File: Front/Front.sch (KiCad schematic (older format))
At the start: 41 parts, among them J1 USB_B_Micro, Q1 BC849, Q2 BC849, SW2 SW_Push, U1 CH340C, U10 ESP32-WROOM-32, U2 CJVL53L0XV2, U3 SPX3819M5-L-3-3

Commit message: V0.2: Redo front schematic and PCB
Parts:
- removed D1: BLUE, LED_SMD:LED_0805_2012Metric_Pad1.15x1.40mm_HandSolder, symbol Device:LED
- removed D2: GREEN, LED_SMD:LED_0805_2012Metric_Pad1.15x1.40mm_HandSolder, symbol Device:LED
- removed H17: VBS, Custom:Mounting_Pad_Power, symbol Front-rescue:MountingPad-Custom
- removed SW2: SW_Push, Button_Switch_SMD:Panasonic_EVQPUJ_EVQPUA, symbol Switch:SW_Push
- added H25: LED1, Custom:Mounting_Pad_Signal, symbol Front-rescue:MountingPad-Custom
- added H26: LED2, Custom:Mounting_Pad_Signal, symbol Front-rescue:MountingPad-Custom
- added H27: TCH2, Custom:Mounting_Pad_Touch, symbol Front-rescue:MountingPad-Custom
- added H28: TCH1, Custom:Mounting_Pad_Touch, symbol Front-rescue:MountingPad-Custom
- added SW1: SW_DPDT_x2, Custom:JS102011SAQN, symbol Switch:SW_DPDT_x2
- H1: value VBUS -> PWR
- H16: value ORST -> O~RST
- R3, R4: value 150 -> 510
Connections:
- net ED_IN1: now also U10.4 (SENSOR_VP); no longer U10.12 (IO27)
- net ED_IN2: now also U10.5 (SENSOR_VN); no longer U10.27 (IO16)
- net M1_AOUT1: now also U10.16 (IO13); no longer U10.19 (SCS/CMD)
- net M1_AOUT2: now also U10.12 (IO27); no longer U10.18 (SWP/SD3)
- net M1_BOUT1: now also U10.13 (IO14); no longer U10.17 (SHD/SD2)
- net M1_BOUT2: now also U10.14 (IO12); no longer U10.16 (IO13)
- net M1_M2_~SLEEP: now also U10.28 (IO17); no longer U10.24 (IO2)
- net M2_AOUT1: now also U10.23 (IO15); no longer U10.20 (SCK/CLK)
- net M2_AOUT2: now also U10.24 (IO2); no longer U10.21 (SDO/SD0)
- net M2_BOUT1: now also U10.26 (IO4); no longer U10.22 (SDI/SD1)
- net M2_BOUT2: now also U10.27 (IO16); no longer U10.23 (IO15)
- net OD_INTERRUPT: now also U10.7 (IO35); no longer U10.31 (IO19)
- net OD_SCL: now also U10.29 (IO5); no longer U10.28 (IO17)
- net OD_SDA: now also U10.30 (IO18); no longer U10.29 (IO5)
- net OD_SHUT: now also U10.31 (IO19); no longer U10.30 (IO18)
- net VBUS: now also SW1.1 (A); no longer U3.1 (IN), U3.3 (EN)
- net LED1: now reaches U10.10 (IO25)
- net LED1: now also H25.1 (Pin)
- net LED2: now reaches U10.11 (IO26)
- net LED2: now also H26.1 (Pin)
- net TOUCH2: now reaches U10.9 (IO33)
- net TOUCH2: now also R4.2
- net TOUCH1: now reaches R3.1
- net TOUCH1: now also U10.8 (IO32)
- net at R4.1: now also H27.1 (Pin)
- net STATUS_LED_BLUE: no longer names the net of R3.2
- net STATUS_LED_BLUE: now also H28.1 (Pin); no longer U10.8 (IO32)
- removed net STATUS_LED_GRN: R4.2, U10.7 (IO35)
- new net: SW1.2 (B), U3.1 (IN), U3.3 (EN)
- no-connect marks 17 -> 16
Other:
- note removed: "Status LEDS"
- moved on the sheet: C2, H1, H10, H11, H12, H13, H14, H15, H16, H18, H19, H2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

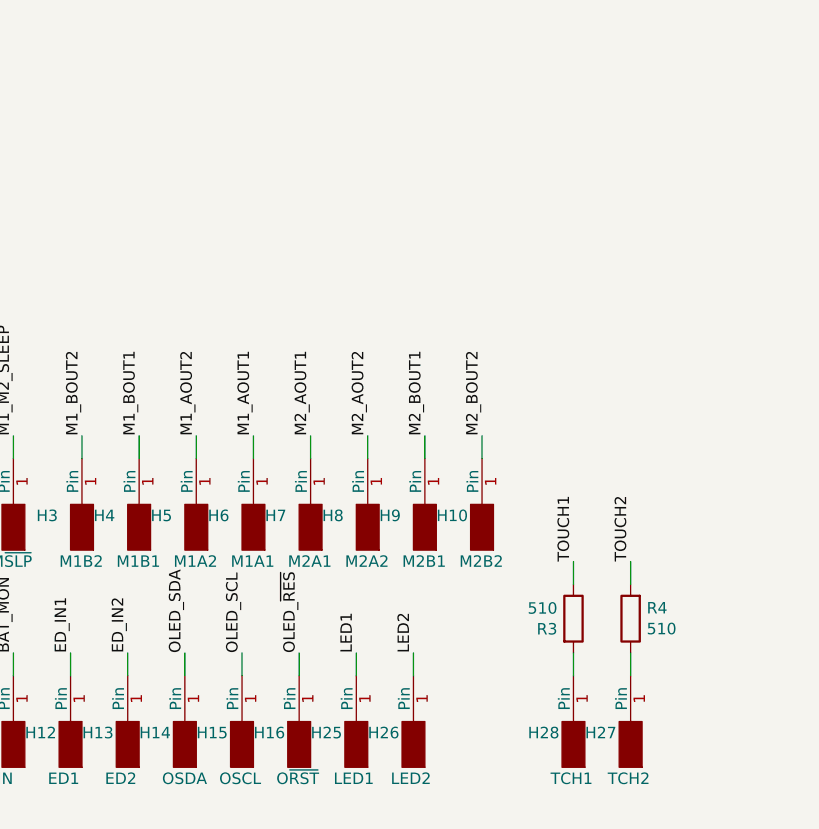
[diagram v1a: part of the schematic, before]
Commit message: finish top, changes to front, added graphic
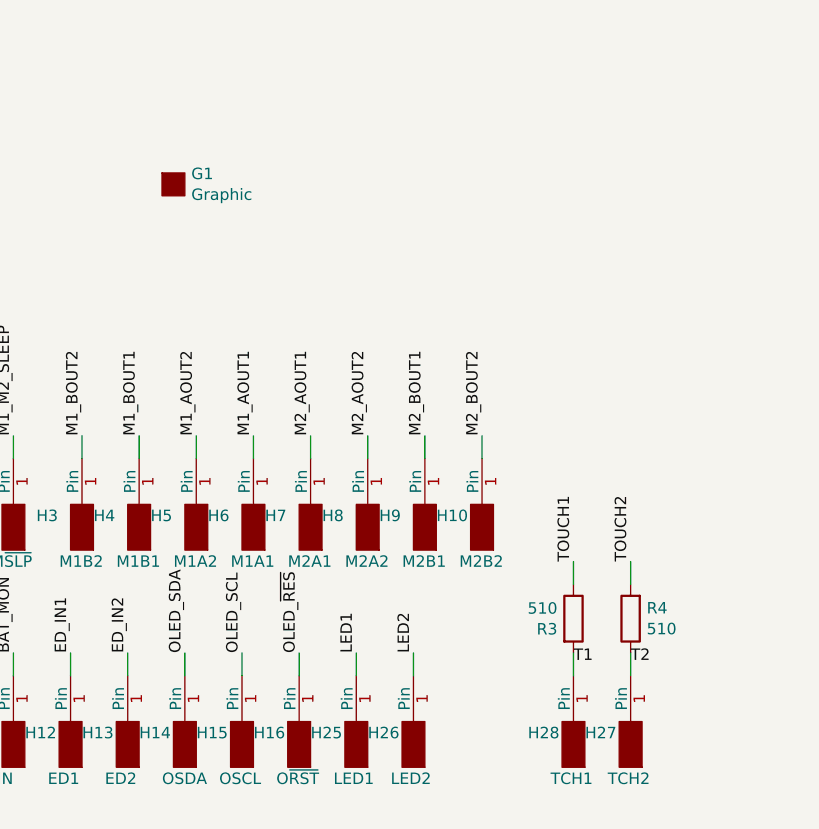
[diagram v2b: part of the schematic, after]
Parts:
- added G1: Graphic, Print:d1, symbol Custom:Graphic
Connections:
- net T2: now reaches H27.1 (Pin), R4.1
- net T1: now reaches H28.1 (Pin), R3.2
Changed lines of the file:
@@
 Text Label 3700 6250 1    50   ~ 0
 TOUCH2
+Text Label 3450 6700 0    50   ~ 0
+T1
+Text Label 3700 6700 0    50   ~ 0
+T2
+$Comp
+L Custom:Graphic G1
+U 1 1 5DEC1C54
+P 1700 4600
+F 0 "G1" H 1778 4646 50  0000 L CNN
+F 1 "Graphic" H 1778 4555 50  0000 L CNN
+F 2 "Print:d1" H 1550 4750 50  0001 C CNN
+F 3 "" H 1550 4750 50  0001 C CNN
+	1    1700 4600
+	1    0    0    -1
+$EndComp
 $EndSCHEMATC

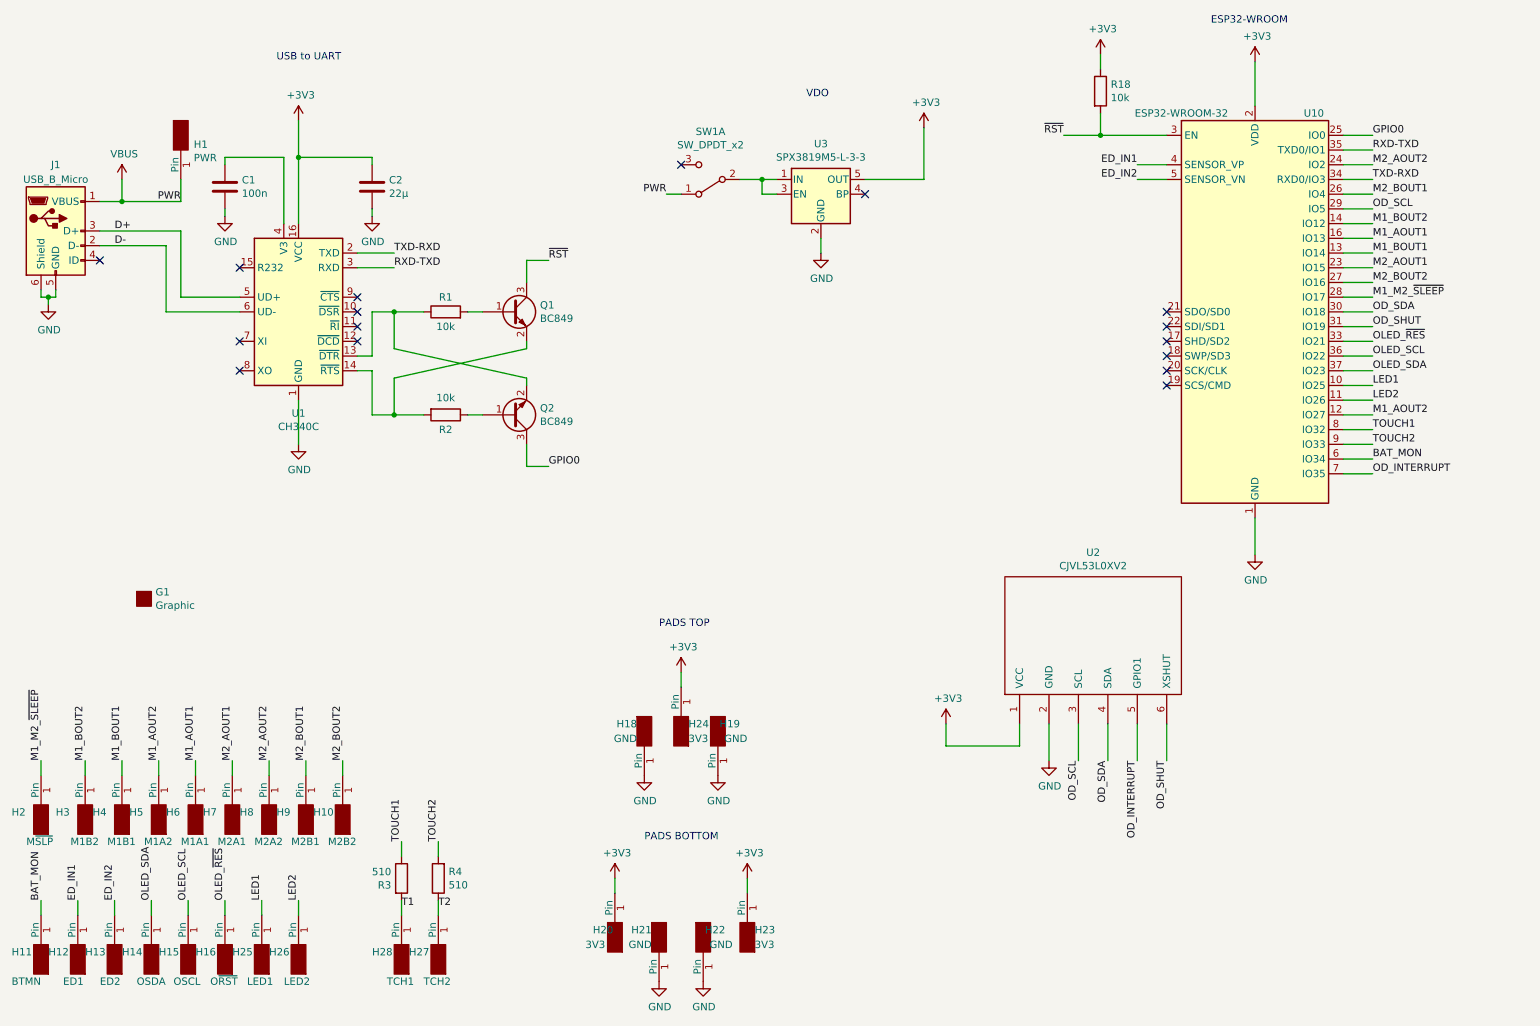
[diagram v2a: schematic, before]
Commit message: removed extra pins in front, respaced pins in bottom and front
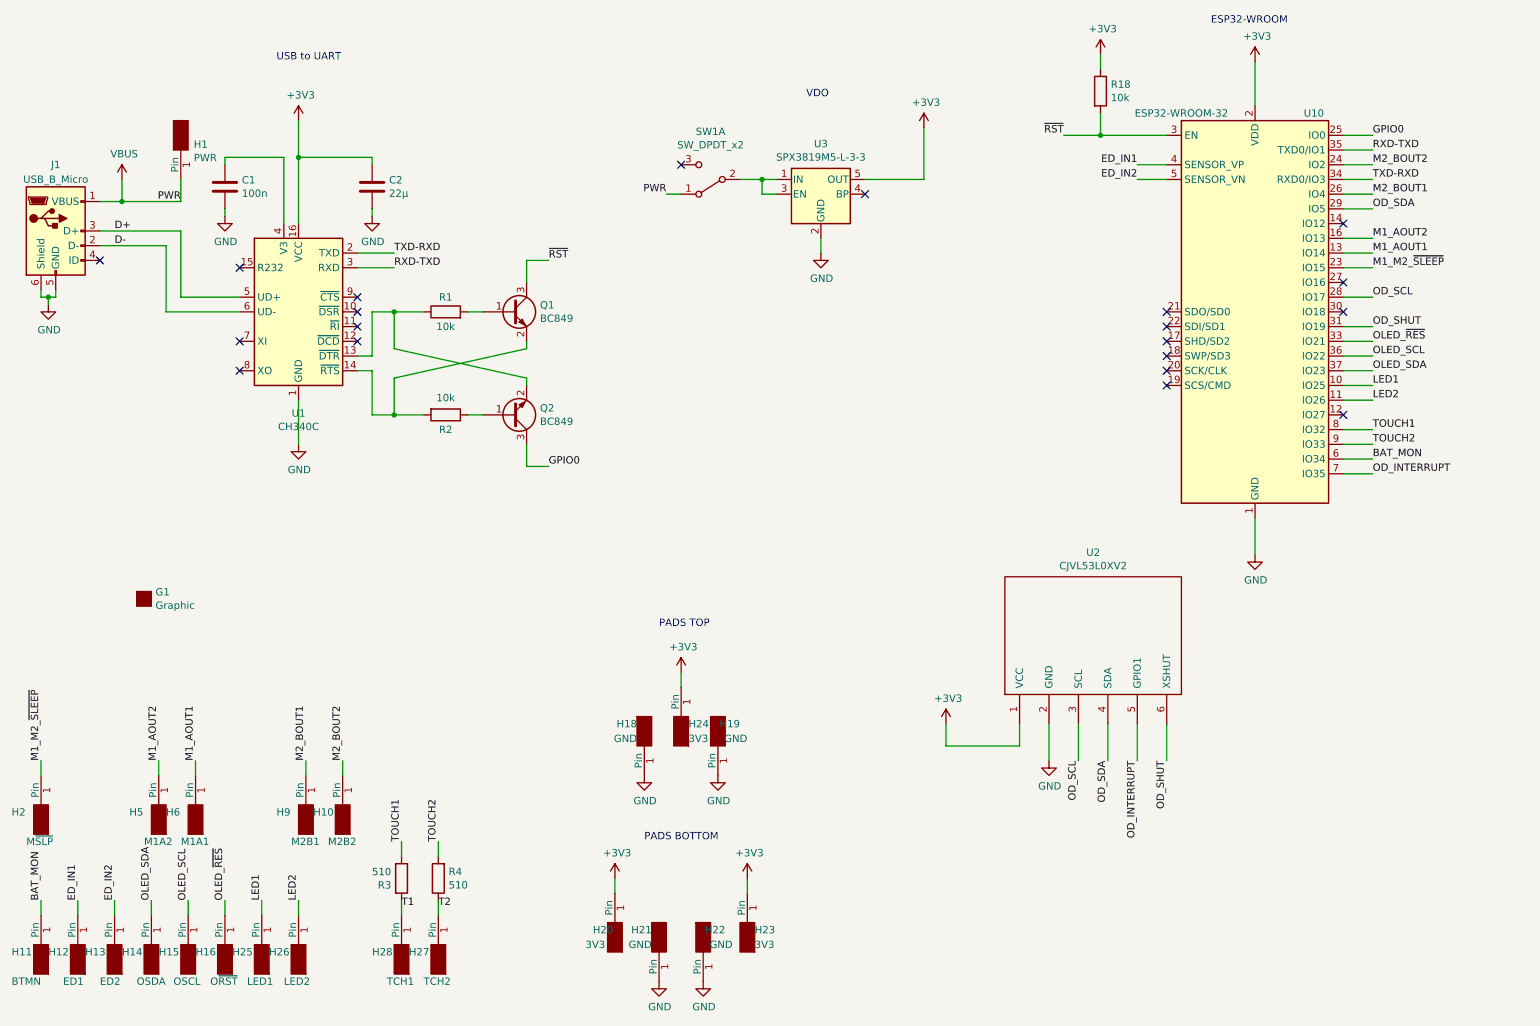
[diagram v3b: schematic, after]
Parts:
- removed H3: M1B2, Custom:Mounting_Pad_Signal, symbol Front-rescue:MountingPad-Custom
- removed H4: M1B1, Custom:Mounting_Pad_Signal, symbol Front-rescue:MountingPad-Custom
- removed H7: M2A1, Custom:Mounting_Pad_Signal, symbol Front-rescue:MountingPad-Custom
- removed H8: M2A2, Custom:Mounting_Pad_Signal, symbol Front-rescue:MountingPad-Custom
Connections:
- net M1_BOUT1 is gone; now on net M1_AOUT1: U10.13 (IO14)
- net M2_AOUT1 is gone; now on net M1_M2_~SLEEP: U10.23 (IO15)
- net M2_AOUT2 is gone; now on net M2_BOUT2: U10.24 (IO2)
- net M1_AOUT1: no longer U10.16 (IO13)
- net M1_AOUT2: now also U10.16 (IO13); no longer U10.12 (IO27)
- net M1_M2_~SLEEP: no longer U10.28 (IO17)
- net M2_BOUT2: no longer U10.27 (IO16)
- net OD_SCL: now also U10.28 (IO17); no longer U10.29 (IO5)
- net OD_SDA: now also U10.29 (IO5); no longer U10.30 (IO18)
- net M1_BOUT2: no longer names the net of U10.14 (IO12)
- no-connect marks 16 -> 20
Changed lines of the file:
@@
 	10050 2850 9850 2850
 Wire Wire Line
-	10050 1650 9850 1650
-Wire Wire Line
-	10050 2150 9850 2150
-Wire Wire Line
-	10050 2350 9850 2350
-Wire Wire Line
 	9850 2750 10050 2750
-Wire Wire Line
-	9850 2650 10050 2650
 Wire Wire Line
 	9850 3050 10050 3050
@@
 Text Label 10050 3150 0    50   ~ 0
 LED1
+Text Label 10050 2550 0    50   ~ 0
+OD_SCL
 Text Label 10050 1950 0    50   ~ 0
-OD_SCL
-Text Label 10050 2650 0    50   ~ 0
 OD_SDA
 Text Label 10050 3750 0    50   ~ 0
@@
 Text Label 10050 2750 0    50   ~ 0
 OD_SHUT
-Text Label 10050 1650 0    50   ~ 0
-M2_AOUT2
-Text Label 10050 1850 0    50   ~ 0
-M2_BOUT1
+Text Label 10050 2150 0    50   ~ 0
+M1_AOUT2
 Text Label 10050 2250 0    50   ~ 0
-M1_BOUT1
-Text Label 10050 3350 0    50   ~ 0
-M1_AOUT2
-Text Label 10050 2350 0    50   ~ 0
-M2_AOUT1
-Text Label 10050 2150 0    50   ~ 0
 M1_AOUT1
 Text Label 8450 1750 2    50   ~ 0
@@
 Text Label 10050 2950 0    50   ~ 0
 OLED_SCL
-Text Label 10050 2450 0    50   ~ 0
+Text Label 10050 1650 0    50   ~ 0
 M2_BOUT2
-Text Label 10050 2050 0    50   ~ 0
-M1_BOUT2
-Text Label 10050 2550 0    50   ~ 0
+Text Label 10050 2350 0    50   ~ 0
 M1_M2_~SLEEP
 Wire Wire Line
@@
 	1    0    0    -1
 $EndComp
-Wire Wire Line
-	9850 3350 10050 3350
-Wire Wire Line
-	9850 2450 10050 2450
 $Comp
 L RF_Module:ESP32-WROOM-32 U10
@@
 Wire Wire Line
 	9850 1950 10050 1950
-Wire Wire Line
-	10050 2550 9850 2550
 Wire Wire Line
 	9850 3750 10050 3750
@@
 OLED_SDA
 Wire Wire Line
-	9850 2050 10050 2050
-Wire Wire Line
-	10050 2250 9850 2250
-Wire Wire Line
 	10050 1850 9850 1850
 Wire Wire Line
@@
 OD_SHUT
 $Comp
-L Front-rescue:MountingPad-Custom H3
-U 1 1 5D86E4E3
-P 1300 6100
-F 0 "H3" H 1500 6050 50  0000 R CNN
-F 1 "M1B2" H 1400 6250 50  0000 R CNN
-F 2 "Custom:Mounting_Pad_Signal" H 1300 6250 50  0001 C CNN
-F 3 "" H 1300 6250 50  0001 C CNN
-	1    1300 6100
-	-1   0    0    1
-$EndComp
-$Comp
-L Front-rescue:MountingPad-Custom H4
-U 1 1 5D86F28C
-P 1550 6100
-F 0 "H4" H 1750 6050 50  0000 R CNN
-F 1 "M1B1" H 1650 6250 50  0000 R CNN
-F 2 "Custom:Mounting_Pad_Signal" H 1550 6250 50  0001 C CNN
-F 3 "" H 1550 6250 50  0001 C CNN
-	1    1550 6100
-	-1   0    0    1
-$EndComp
-$Comp
 L Front-rescue:MountingPad-Custom H5
 U 1 1 5D86F5DD
@@
 $EndComp
 $Comp
-L Front-rescue:MountingPad-Custom H7
-U 1 1 5D86FB12
-P 2300 6100
-F 0 "H7" H 2500 6050 50  0000 R CNN
-F 1 "M2A1" H 2400 6250 50  0000 R CNN
-F 2 "Custom:Mounting_Pad_Signal" H 2300 6250 50  0001 C CNN
-F 3 "" H 2300 6250 50  0001 C CNN
-	1    2300 6100
-	-1   0    0    1
-$EndComp
-$Comp
-L Front-rescue:MountingPad-Custom H8
-U 1 1 5D86FE2A
-P 2550 6100
-F 0 "H8" H 2750 6050 50  0000 R CNN
-F 1 "M2A2" H 2650 6250 50  0000 R CNN
-F 2 "Custom:Mounting_Pad_Signal" H 2550 6250 50  0001 C CNN
-F 3 "" H 2550 6250 50  0001 C CNN
-	1    2550 6100
-	-1   0    0    1
-$EndComp
-$Comp
 L Front-rescue:MountingPad-Custom H9
 U 1 1 5D870117
@@
 	-1   0    0    1
 $EndComp
-Text Label 1300 5700 1    50   ~ 0
-M1_BOUT2
-Text Label 1550 5700 1    50   ~ 0
-M1_BOUT1
 Text Label 1800 5700 1    50   ~ 0
 M1_AOUT2
 Text Label 2050 5700 1    50   ~ 0
 M1_AOUT1
-Text Label 2300 5700 1    50   ~ 0
-M2_AOUT1
-Text Label 2550 5700 1    50   ~ 0
-M2_AOUT2
 Text Label 2800 5700 1    50   ~ 0
 M2_BOUT1
@@
 M2_BOUT2
 Wire Wire Line
-	1300 5700 1300 5800
-Wire Wire Line
-	1550 5700 1550 5800
-Wire Wire Line
 	1800 5700 1800 5800
 Wire Wire Line
 	2050 5700 2050 5800
-Wire Wire Line
-	2300 5700 2300 5800
-Wire Wire Line
-	2550 5700 2550 5800
 Wire Wire Line
 	2800 5700 2800 5800
@@
 	1    0    0    -1
 $EndComp
+Wire Wire Line
+	9850 2250 10050 2250
+Wire Wire Line
+	10050 2150 9850 2150
+Text Label 10050 1850 0    50   ~ 0
+M2_BOUT1
+Wire Wire Line
+	10050 2350 9850 2350
+Wire Wire Line
+	9850 1650 10050 1650
+NoConn ~ 9850 3350
+NoConn ~ 9850 2450
+NoConn ~ 9850 2050
+Wire Wire Line
+	10050 2550 9850 2550
+NoConn ~ 9850 2650
 $EndSCHEMATC
